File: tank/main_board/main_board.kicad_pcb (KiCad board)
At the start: 2 copper layers, 71.5 x 61.5 mm, 40 parts, among them J1 Encoder0, J10 PowerMotor, J11 M0, J12 M1, J13 M2, J14 Spk, J15 LEDs, J16 SigOut, J2 Encoder1, J3 Encoder2, J4 Encoder3, J5 Programming Header, J6 Bump0, J7 Bump1, J8 PowerOut, J9 PowerIn, U1 L7805, U2 ATMEGA328P-PU, U3 SN74HC595, U4 L293D, U5 L293D, Y1 Crystal

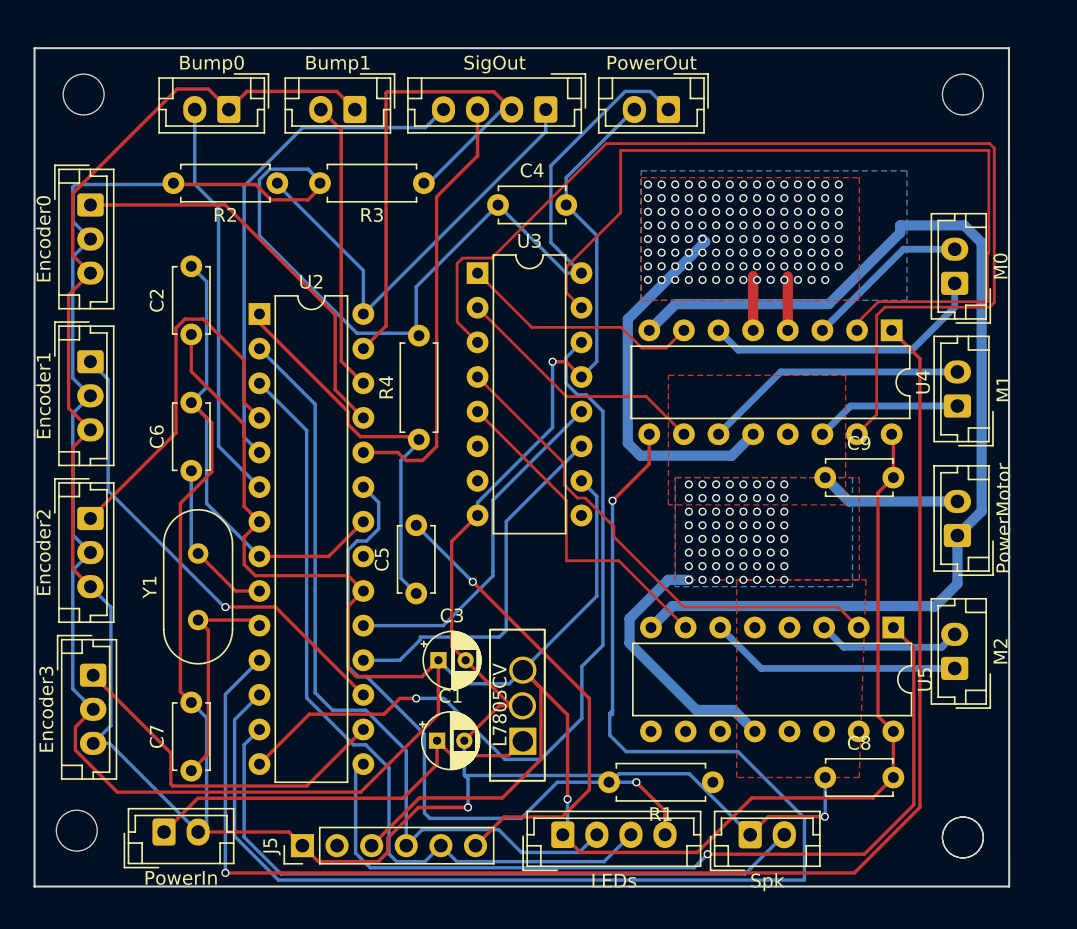
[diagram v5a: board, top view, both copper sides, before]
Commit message: Main Board v0.15
Changes:
    - back to L293 motor driver
    - add speaker resistor
    - 3.5mm pitch screw terminals for motors and motor power
    - move programming header
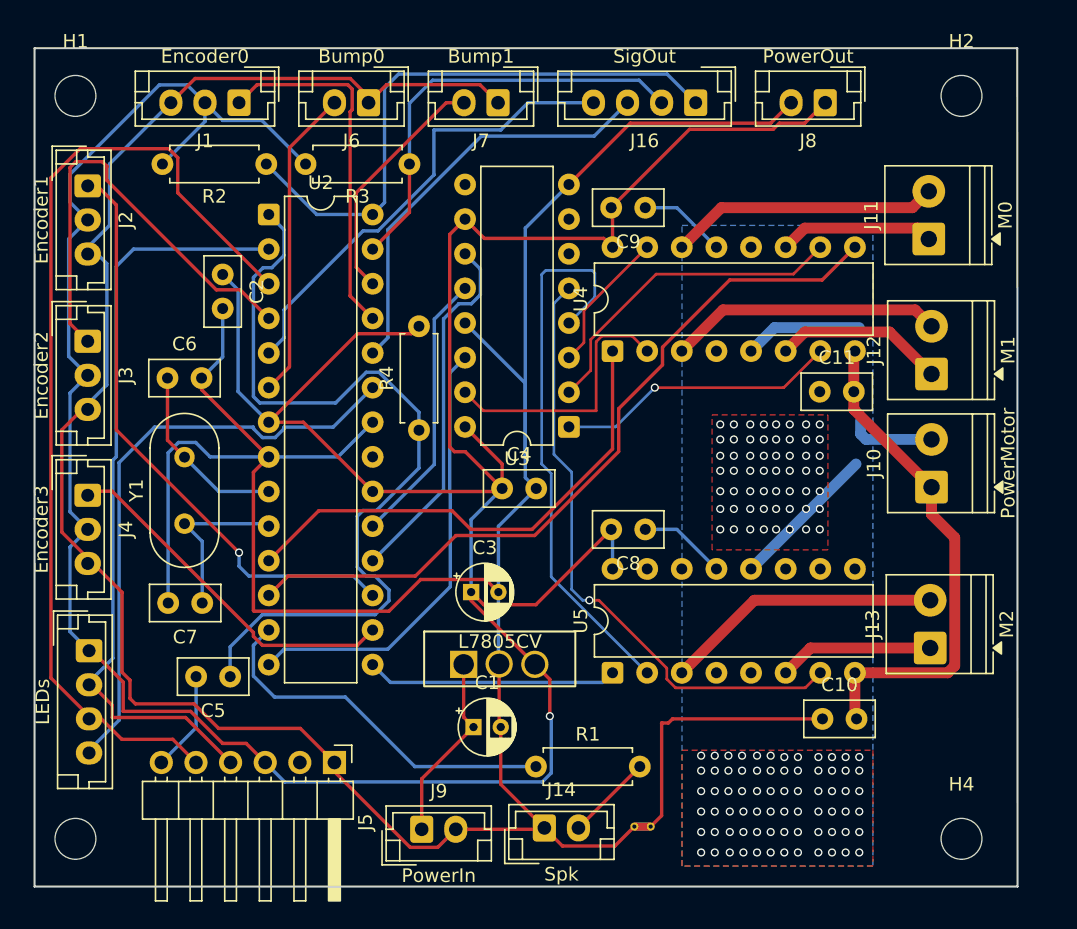
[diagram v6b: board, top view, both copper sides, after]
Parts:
- removed ?: , 
- removed REF** (x4): MountingHole_3mm, custom:MountingHole_3mm
- added C10: .1uF, Capacitor_THT:C_Disc_D5.0mm_W2.5mm_P2.50mm, F.Cu at (148.8, 122.2)
- added C11: .1uF, Capacitor_THT:C_Disc_D5.0mm_W2.5mm_P2.50mm, F.Cu at (148.6, 98.2)
- added G***: LOGO, custom:Tank, B.Cu at (143.8, 126.5)
- added H1: MountingHole, MountingHole:MountingHole_3mm, F.Cu at (94.0, 76.5)
- added H2: MountingHole, MountingHole:MountingHole_3mm, F.Cu at (159.0, 76.5)
- added H3: MountingHole, MountingHole:MountingHole_3mm, F.Cu at (94.0, 131.0)
- added H4: MountingHole, MountingHole:MountingHole_3mm, F.Cu at (159.0, 131.0)
- added NT1: NetTie_2, NetTie:NetTie-2_THT_Pad0.3mm, F.Cu at (136.2, 130.1)
- C1, C3: footprint custom:CP_Radial_D4.0mm_P2.00mm -> Capacitor_THT:CP_Radial_D4.0mm_P2.00mm
- C2, C4, C5, C6, C7, C8, C9: footprint custom:C_Disc_D4.7mm_W2.5mm_P5.00mm -> Capacitor_THT:C_Disc_D5.0mm_W2.5mm_P2.50mm
- J1, J2, J3, J4: footprint custom:JST_EH_B3B-EH-A_1x03_P2.50mm_Vertical -> Connector_JST:JST_EH_B3B-EH-A_1x03_P2.50mm_Vertical
- J10, J11, J12, J13: footprint custom:JST_EH_B2B-EH-A_1x02_P2.50mm_Vertical -> TerminalBlock_Phoenix:TerminalBlock_Phoenix_PT-1,5-2-3.5-H_1x02_P3.50mm_Horizontal
- J14, J6, J7, J8, J9: footprint custom:JST_EH_B2B-EH-A_1x02_P2.50mm_Vertical -> Connector_JST:JST_EH_B2B-EH-A_1x02_P2.50mm_Vertical
- J15, J16: footprint custom:JST_EH_B4B-EH-A_1x04_P2.50mm_Vertical -> Connector_JST:JST_EH_B4B-EH-A_1x04_P2.50mm_Vertical
- J5: footprint custom:PinHeader_1x06_P2.54mm_Vertical -> Connector_PinHeader_2.54mm:PinHeader_1x06_P2.54mm_Horizontal
- R1: value 10k -> R; footprint custom:R_Axial_DIN0207_L6.3mm_D2.5mm_P7.62mm_Horizontal -> Resistor_THT:R_Axial_DIN0207_L6.3mm_D2.5mm_P7.62mm_Horizontal
- R2, R3, R4: footprint custom:R_Axial_DIN0207_L6.3mm_D2.5mm_P7.62mm_Horizontal -> Resistor_THT:R_Axial_DIN0207_L6.3mm_D2.5mm_P7.62mm_Horizontal
- U2: footprint custom:DIP-28_W7.62mm -> Package_DIP:DIP-28_W7.62mm
- U3, U4, U5: footprint custom:DIP-16_W7.62mm -> Package_DIP:DIP-16_W7.62mm
- moved J15 37.3 mm to (95.0, 117.2), turned to -90 degrees
- moved C9 23.8 mm to (135.8, 84.7), turned to 180 degrees
- moved C8 22.5 mm to (135.8, 108.3), turned to 180 degrees
- moved U5 20.9 mm to (133.4, 118.8), turned to 90 degrees
- moved C4 20.8 mm to (125.3, 105.3)
- moved U4 20.5 mm to (133.4, 95.2), turned to 90 degrees
- moved J9 18.9 mm to (119.4, 130.3)
- moved J14 15.1 mm to (128.4, 130.2)
- moved C5 15.0 mm to (105.3, 119.1), turned to 180 degrees
- moved J1 13.2 mm to (106.0, 77.0), turned to 180 degrees
- moved J4 13.2 mm to (94.9, 105.8)
- moved U3 13.1 mm to (130.2, 100.8), turned to 180 degrees
- moved R1 13.0 mm to (127.8, 125.7), turned to 0 degrees
- moved J3 13.0 mm to (94.9, 94.5)
- moved J2 12.9 mm to (94.9, 83.1)
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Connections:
- C5 pad 1: Net-(C5-Pad1) -> Net-(U2-(PCINT14/~{RESET})PC6)
- J11 pad 1: Net-(J11-Pad1) -> Net-(J11-Pin_1)
- J11 pad 2: Net-(J11-Pad2) -> Net-(J11-Pin_2)
- J12 pad 1: Net-(J12-Pad1) -> Net-(J12-Pin_1)
- J12 pad 2: Net-(J12-Pad2) -> Net-(J12-Pin_2)
- R1 pad 1: (no net) -> Net-(U2-(PCINT23/AIN1)PD7)
- R1 pad 2: (no net) -> SPK
- R2 pad 1: (no net) -> SCL
- R2 pad 2: (no net) -> 4.5V
- R3 pad 1: (no net) -> SDA
- R3 pad 2: (no net) -> 4.5V
- R4 pad 1: (no net) -> Net-(U2-(PCINT14/~{RESET})PC6)
- R4 pad 2: (no net) -> 4.5V
- U2 pad 1: Net-(C5-Pad1) -> Net-(U2-(PCINT14/~{RESET})PC6)
- U2 pad 13: Net-(R1-Pad1) -> Net-(U2-(PCINT23/AIN1)PD7)
- U4 pad 11: Net-(J12-Pad2) -> Net-(J11-Pin_1)
- U4 pad 14: Net-(J12-Pad1) -> Net-(J11-Pin_2)
- U4 pad 3: Net-(J11-Pad2) -> Net-(J12-Pin_2)
- U4 pad 6: Net-(J11-Pad1) -> Net-(J12-Pin_1)
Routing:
- net M1-: track 79.2 -> 10.5 mm
- net M0PWM: track 105.4 -> 36.9 mm, vias 1 -> 0
- net 4.5V: track 319.9 -> 253.6 mm
- net Net-(U2-(PCINT14/~{RESET})PC6): track 0.00 -> 62.5 mm
- net M2PWM: track 63.7 -> 18.4 mm, vias 1 -> 0
- net SPK: track 50.3 -> 6.36 mm
- net M1PWM: track 99.2 -> 56.2 mm, vias 1 -> 0
- net M0+: track 62.5 -> 19.6 mm
- net Vm: track 77.9 -> 37.2 mm
- net Net-(C5-Pad1): track 28.2 -> 0.00 mm
- net Net-(J5-Pin_6): track 34.7 -> 7.36 mm, vias 1 -> 0
- net Net-(U2-(PCINT23/AIN1)PD7): track 0.00 -> 27.3 mm
- net SERIAL_DATA: track 58.9 -> 33.0 mm, vias 1 -> 0
- net Net-(J11-Pad1): track 21.0 -> 0.00 mm
- net M2-: track 24.4 -> 45.2 mm, vias 0 -> 1
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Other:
- board size 71.5 x 61.5 mm -> 72.1 x 61.5 mm
- board text added: "Main Board v0.15 Laser Tag Robot Tank M.I.A.R. Labs nick.groesz@gmail.com"
- board text removed: "Main Board v0.12 Laser Tag Robot Tank M.I.A.R. Labs nick.groesz@gmail.com"

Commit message: IR Camera v0.2
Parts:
- removed G***: LOGO, custom:Tank
- added Q1: NPN, Package_TO_SOT_THT:TO-92, F.Cu at (130.7, 123.4)
- moved R1 10.9 mm to (136.3, 132.5), turned to 90 degrees
- moved NT1 4.43 mm to (140.1, 132.2)
- renumbered C9 to C8, C8 to C9, H4 to H2, H2 to H4, J14 to J11, J15 to J12, J16 to J13, J13 to J14, J12 to J15, J11 to J16, J3 to J2, J4 to J3, J5 to J4, J2 to J5, U5 to U4, U4 to U5
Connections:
- J11 pad 2: SPK -> Net-(J11-Pin_2)
- R1 pad 1: Net-(U2-(PCINT23/AIN1)PD7) -> SPK
- R1 pad 2: SPK -> Net-(Q1-B)
- U2 pad 13: Net-(U2-(PCINT23/AIN1)PD7) -> SPK
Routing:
- net 4.5V: track 253.6 -> 224.8 mm, vias 1 -> 0
- net Net-(U2-(PCINT23/AIN1)PD7): track 27.3 -> 0.00 mm
- net SPK: track 6.36 -> 27.3 mm
- net Gm: track 58.6 -> 38.8 mm, vias 128 -> 116
- net GND: track 275.0 -> 267.2 mm

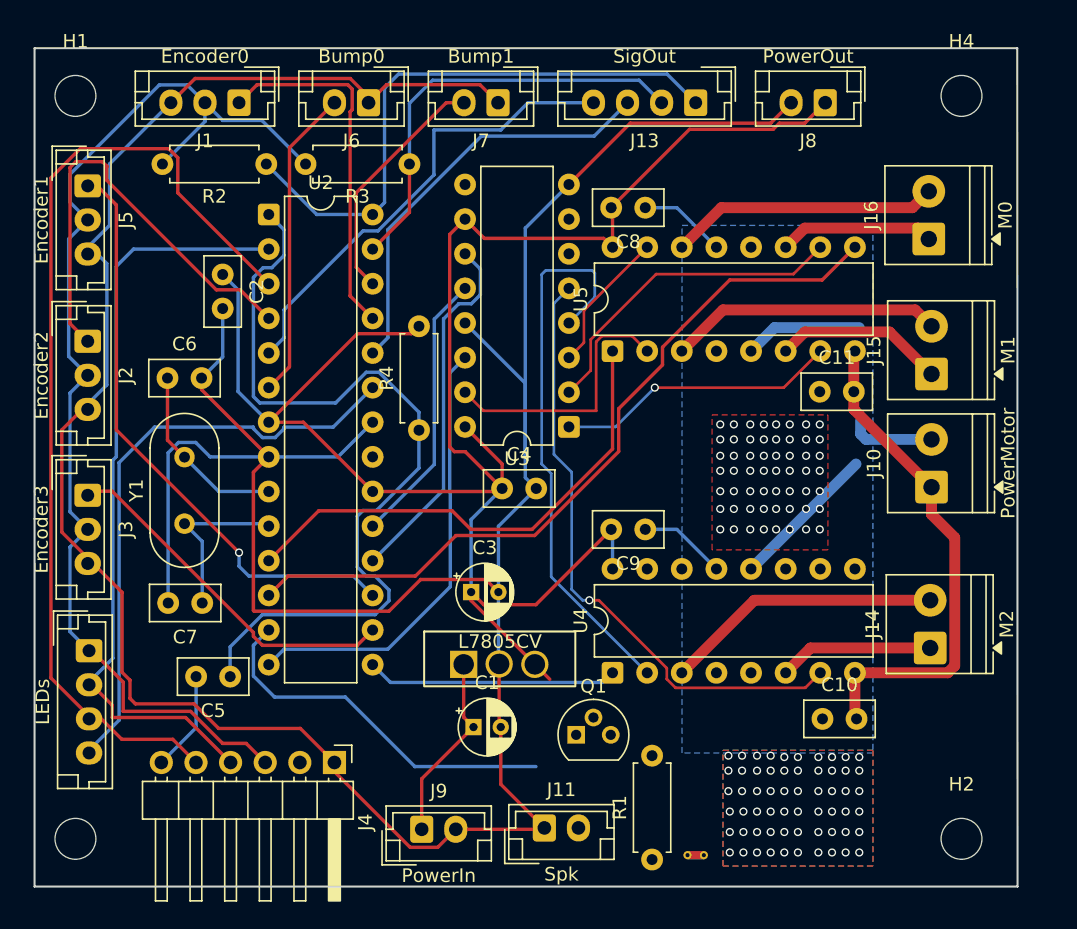
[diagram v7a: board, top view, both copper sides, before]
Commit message: updates for a new version of main board, mostly just KiCAD fixes but this also includes a transistor for the speaker
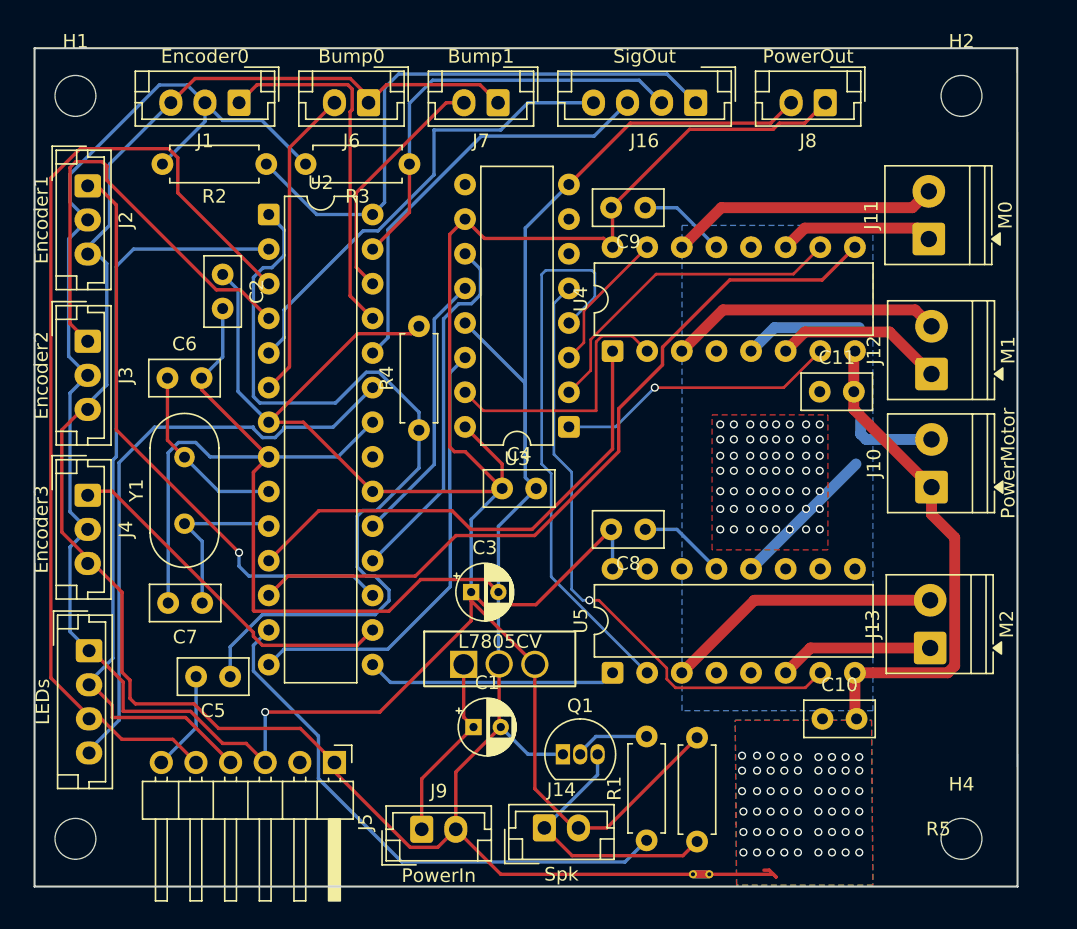
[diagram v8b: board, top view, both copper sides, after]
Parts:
- added R5: R, Resistor_THT:R_Axial_DIN0207_L6.3mm_D2.5mm_P7.62mm_Horizontal, F.Cu at (139.6, 123.6)
- Q1: value NPN -> 2N3904; footprint Package_TO_SOT_THT:TO-92 -> Package_TO_SOT_THT:TO-92_Inline
- moved Q1 1.73 mm to (129.8, 124.8)
- moved R1 1.47 mm to (135.9, 131.1)
- moved NT1 1.46 mm to (140.5, 133.6)
- renumbered C9 to C8, C8 to C9, H4 to H2, H2 to H4, J16 to J11, J15 to J12, J14 to J13, J11 to J14, J12 to J15, J13 to J16, J5 to J2, J2 to J3, J3 to J4, J4 to J5, U5 to U4, U4 to U5
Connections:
- J14 pad 1: GND -> Net-(J14-Pin_1)
- J14 pad 2: Net-(J11-Pin_2) (its old number) -> 4.5V
- Q1 pad 1: 4.5V -> GND
- Q1 pad 3: Net-(J11-Pin_2) (its old number) -> Net-(J14-Pin_1)
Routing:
- net 4.5V: track 224.8 -> 272.0 mm, vias 0 -> 1
- net Net-(J14-Pin_1): track 0.00 -> 19.6 mm
- net GND: track 267.2 -> 285.0 mm
- net SPK: track 27.3 -> 40.6 mm
- net Gm: track 38.8 -> 44.8 mm, vias 116 -> 110
- net Net-(Q1-B): track 0.00 -> 5.51 mm
